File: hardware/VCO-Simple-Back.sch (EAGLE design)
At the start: 85 parts, among them IC1 TL071, IC2 V3340SO16, IC3 LM397, IC4 TL072, IC5 TL072, P1 POWER_SIMPLE10_SHROUDED, Q1 3904, Q2 3904, U1 LM79L05A, U2 MC78L05A

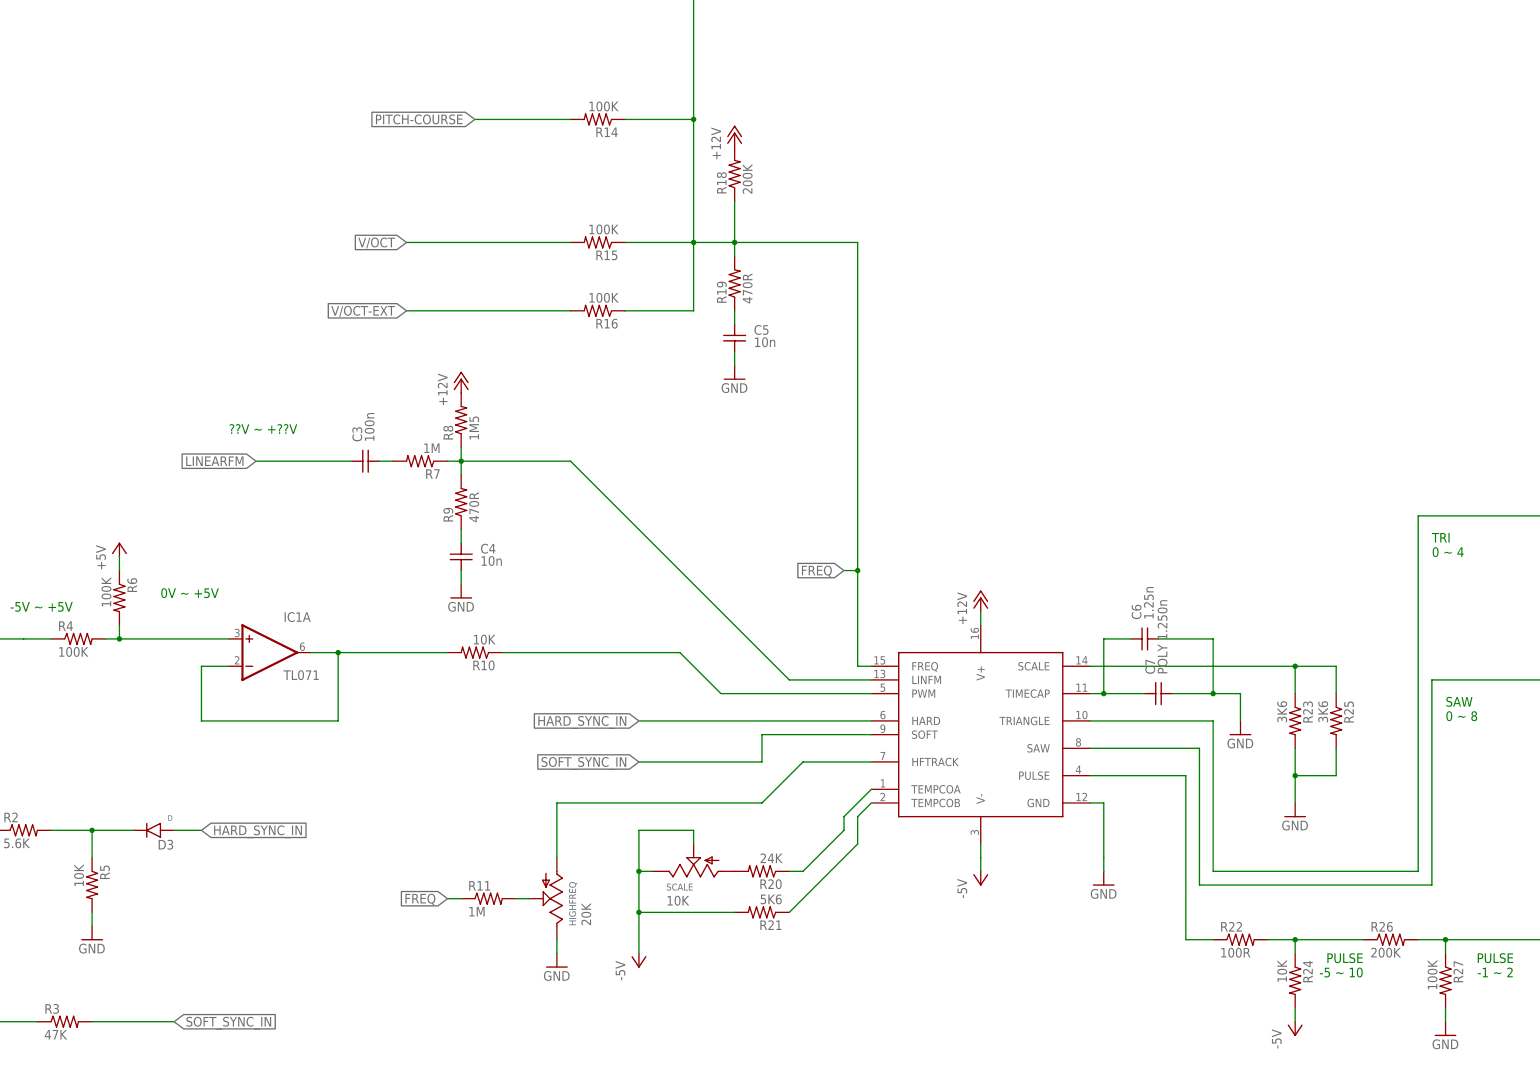
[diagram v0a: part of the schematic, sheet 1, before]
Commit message: revised component values
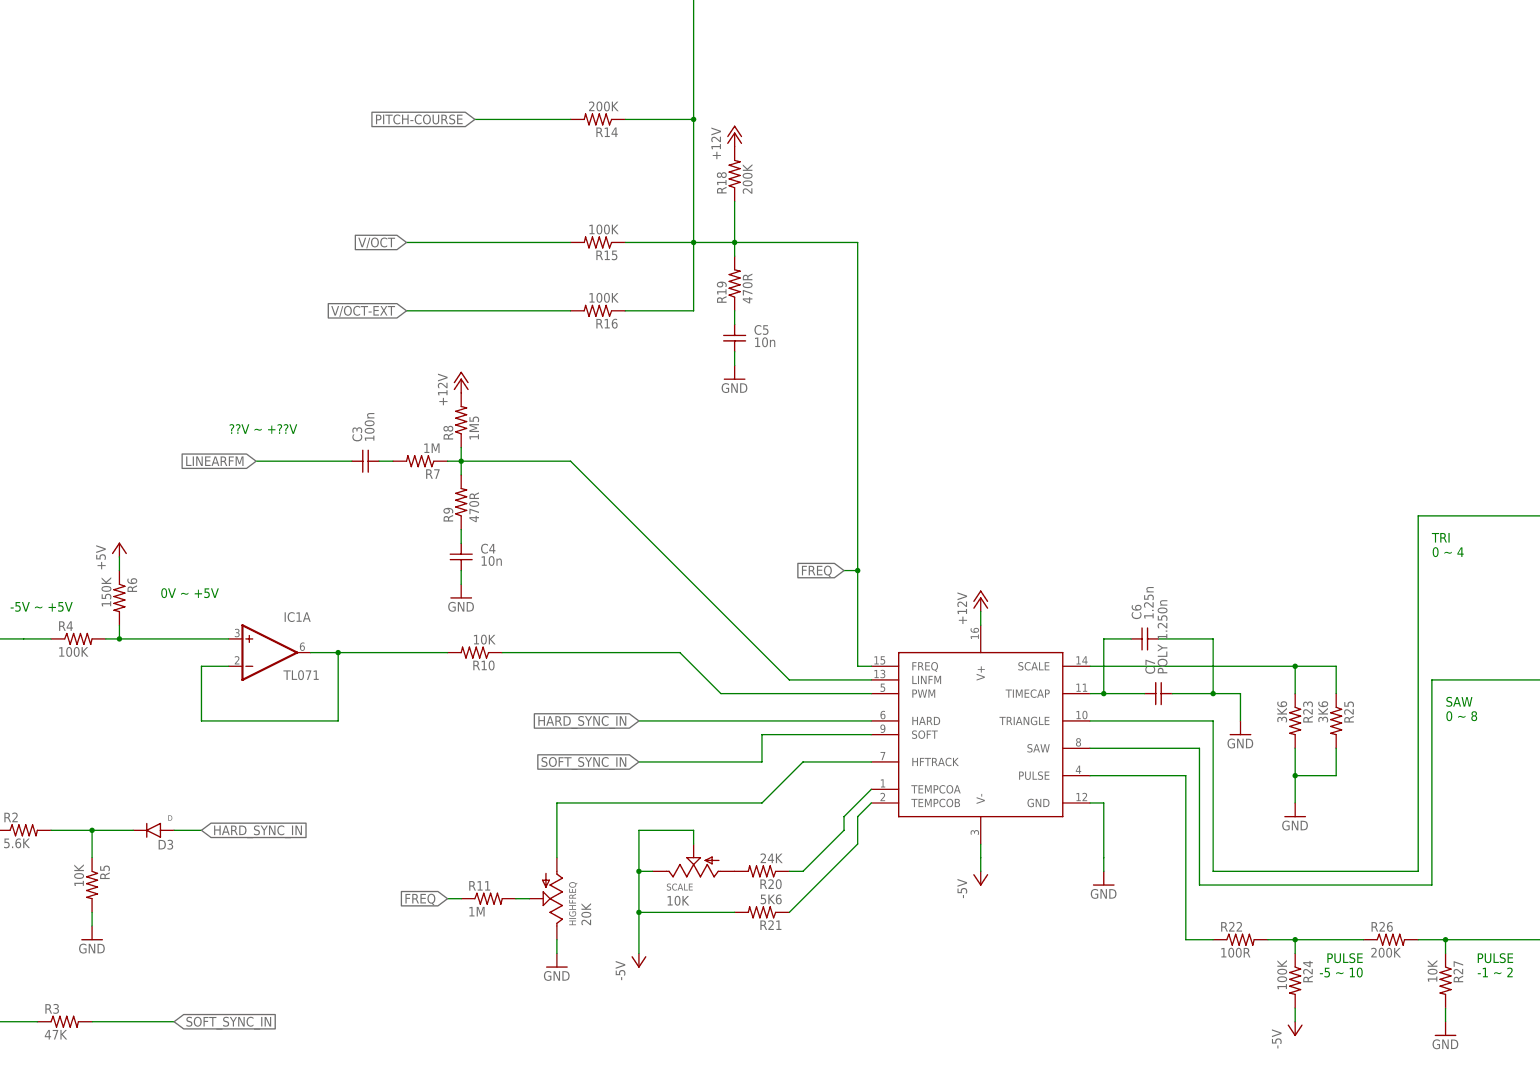
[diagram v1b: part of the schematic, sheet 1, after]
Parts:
- DRIVE, R24: value 10K -> 100K
- R14: value 100K -> 200K
- R27: value 100K -> 10K
- R32: value 10K -> 1K
- R6: value 100K -> 150K
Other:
- note removed: "CHECK VALUER"
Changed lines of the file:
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@@
 <part name="P-3" library="supply1" library_urn="urn:adsk.eagle:library:371" deviceset="-5V" device=""/>
 <part name="P-2" library="supply1" library_urn="urn:adsk.eagle:library:371" deviceset="-5V" device=""/>
-<part name="R24" library="barsstronics" deviceset="RESISTOR" device="0805" value="10K"/>
-<part name="R14" library="barsstronics" deviceset="RESISTOR" device="0805" value="100K"/>
+<part name="R24" library="barsstronics" deviceset="RESISTOR" device="0805" value="100K"/>
+<part name="R14" library="barsstronics" deviceset="RESISTOR" device="0805" value="200K"/>
 <part name="P-4" library="supply1" library_urn="urn:adsk.eagle:library:371" deviceset="-5V" device=""/>
 <part name="R22" library="barsstronics" deviceset="RESISTOR" device="0805" value="100R"/>
@@
 <part name="SCALE" library="barsstronics" deviceset="POT" device="TRIM-MULTITURN-VERT" value="10K"/>
 <part name="R10" library="barsstronics" deviceset="RESISTOR" device="0805" value="10K"/>
-<part name="R27" library="barsstronics" deviceset="RESISTOR" device="0805" value="100K"/>
+<part name="R27" library="barsstronics" deviceset="RESISTOR" device="0805" value="10K"/>
 <part name="R26" library="barsstronics" deviceset="RESISTOR" device="0805" value="200K"/>
 <part name="R13" library="barsstronics" deviceset="RESISTOR" device="0805" value="1M"/>
@@
 <part name="R1" library="barsstronics" deviceset="RESISTOR" device="0805" value="100R"/>
 <part name="R4" library="barsstronics" deviceset="RESISTOR" device="0805" value="100K"/>
-<part name="R6" library="barsstronics" deviceset="RESISTOR" device="0805" value="100K"/>
+<part name="R6" library="barsstronics" deviceset="RESISTOR" device="0805" value="150K"/>
 <part name="P+2" library="supply1" library_urn="urn:adsk.eagle:library:371" deviceset="+5V" device=""/>
 <part name="IC1" library="barsstronics" deviceset="OPAMP-SINGLE" device="" value="TL071"/>
@@
 <part name="R30" library="barsstronics" deviceset="RESISTOR" device="0805" value="100K"/>
 <part name="R31" library="barsstronics" deviceset="RESISTOR" device="0805" value="200K"/>
-<part name="R32" library="barsstronics" deviceset="RESISTOR" device="0805" value="10K"/>
+<part name="R32" library="barsstronics" deviceset="RESISTOR" device="0805" value="1K"/>
 <part name="IC4" library="barsstronics" deviceset="OPAMP-DUAL" device="" value="TL072"/>
 <part name="C12" library="barsstronics" deviceset="CAPACITOR" device="0805" value="100n"/>
@@
 <part name="R40" library="barsstronics" deviceset="RESISTOR" device="0805" value="2K2"/>
 <part name="R34" library="barsstronics" deviceset="RESISTOR" device="0805" value="2K2"/>
-<part name="DRIVE" library="barsstronics" deviceset="POT" device="TRIM-MULTITURN-VERT" value="10K"/>
+<part name="DRIVE" library="barsstronics" deviceset="POT" device="TRIM-MULTITURN-VERT" value="100K"/>
 <part name="SYMMETRY" library="barsstronics" deviceset="POT" device="TRIM-MULTITURN-VERT" value="50K"/>
 <part name="GND12" library="supply1" library_urn="urn:adsk.eagle:library:371" deviceset="GND" device=""/>
@@
 <description>WAVESHAPING</description>
 <plain>
-<text x="182.88" y="78.74" size="1.778" layer="91">CHECK VALUER</text>
 </plain>
 <instances>
